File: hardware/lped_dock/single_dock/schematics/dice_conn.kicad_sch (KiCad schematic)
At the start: 3 parts, among them J1 V_{OUT}, J2 CONN, J3 GND

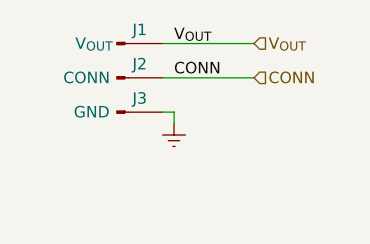
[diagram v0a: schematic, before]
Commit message: feat(hardware): add battery charger and connector to single charger
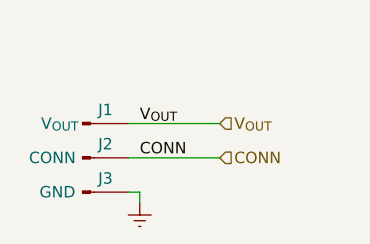
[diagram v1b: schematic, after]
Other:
- moved on the sheet: J1, J2, J3
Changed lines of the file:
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@@
 	(wire
 		(pts
-			(xy 133.35 91.44) (xy 134.62 91.44)
+			(xy 129.54 92.71) (xy 139.7 92.71)
 		)
 		(stroke
@@
 	(wire
 		(pts
-			(xy 143.51 87.63) (xy 133.35 87.63)
+			(xy 139.7 96.52) (xy 129.54 96.52)
 		)
 		(stroke
@@
 	(wire
 		(pts
-			(xy 133.35 83.82) (xy 143.51 83.82)
+			(xy 130.81 100.33) (xy 130.81 101.6)
 		)
 		(stroke
@@
 	(wire
 		(pts
-			(xy 134.62 91.44) (xy 134.62 92.71)
+			(xy 129.54 100.33) (xy 130.81 100.33)
 		)
 		(stroke
@@
 		)
 	)
-	(label "CONN"
-		(at 134.62 87.63 0)
+	(label "V_{OUT}"
+		(at 130.81 92.71 0)
 		(effects
 			(font
@@
 		)
 	)
-	(label "V_{OUT}"
-		(at 134.62 83.82 0)
+	(label "CONN"
+		(at 130.81 96.52 0)
 		(effects
 			(font
@@
 		)
 	)
-	(hierarchical_label "V_{OUT}"
+	(hierarchical_label "CONN"
 		(shape input)
-		(at 143.51 83.82 0)
+		(at 139.7 96.52 0)
 		(effects
 			(font
@@
 		)
 	)
-	(hierarchical_label "CONN"
+	(hierarchical_label "V_{OUT}"
 		(shape input)
-		(at 143.51 87.63 0)
+		(at 139.7 92.71 0)
 		(effects
 			(font
@@
 	(symbol
 		(lib_id "Connector:Conn_01x01_Pin")
-		(at 128.27 87.63 0)
+		(at 124.46 96.52 0)
 		(unit 1)
 		(exclude_from_sim no)
@@
 		(dnp no)
 		(property "Reference" "J2"
-			(at 130.81 86.106 0)
+			(at 127 94.996 0)
 			(effects
 				(font
@@
 		)
 		(property "Value" "CONN"
-			(at 127.508 87.63 0)
+			(at 123.698 96.52 0)
 			(effects
 				(font
@@
 		)
 		(property "Footprint" "Connector_Pin:Pin_D0.9mm_L10.0mm_W2.4mm_FlatFork"
-			(at 128.27 87.63 0)
+			(at 124.46 96.52 0)
 			(effects
 				(font
@@
 		)
 		(property "Datasheet" "~"
-			(at 128.27 87.63 0)
+			(at 124.46 96.52 0)
 			(effects
 				(font
@@
 		)
 		(property "Description" "Generic connector, single row, 01x01, script generated"
-			(at 128.27 87.63 0)
+			(at 124.46 96.52 0)
 			(effects
 				(font
@@
 	(symbol
 		(lib_id "Connector:Conn_01x01_Pin")
-		(at 128.27 83.82 0)
+		(at 124.46 92.71 0)
 		(unit 1)
 		(exclude_from_sim no)
@@
 		(dnp no)
 		(property "Reference" "J1"
-			(at 130.81 82.296 0)
+			(at 127 91.186 0)
 			(effects
 				(font
@@
 		)
 		(property "Value" "V_{OUT}"
-			(at 125.73 83.82 0)
+			(at 121.92 92.71 0)
 			(effects
 				(font
@@
 		)
 		(property "Footprint" "Connector_Pin:Pin_D0.9mm_L10.0mm_W2.4mm_FlatFork"
-			(at 128.27 83.82 0)
+			(at 124.46 92.71 0)
 			(effects
 				(font
@@
 		)
 		(property "Datasheet" "~"
-			(at 128.27 83.82 0)
+			(at 124.46 92.71 0)
 			(effects
 				(font
@@
 		)
 		(property "Description" "Generic connector, single row, 01x01, script generated"
-			(at 128.27 83.82 0)
+			(at 124.46 92.71 0)
 			(effects
 				(font
@@
 	(symbol
 		(lib_id "Connector:Conn_01x01_Pin")
-		(at 128.27 91.44 0)
+		(at 124.46 100.33 0)
 		(unit 1)
 		(exclude_from_sim no)
@@
 		(dnp no)
 		(property "Reference" "J3"
-			(at 130.81 89.916 0)
+			(at 127 98.806 0)
 			(effects
 				(font
@@
 		)
 		(property "Value" "GND"
-			(at 125.476 91.44 0)
+			(at 121.666 100.33 0)
 			(effects
 				(font
@@
 		)
 		(property "Footprint" "Connector_Pin:Pin_D0.9mm_L10.0mm_W2.4mm_FlatFork"
-			(at 128.27 91.44 0)
+			(at 124.46 100.33 0)
 			(effects
 				(font
@@
 		)
 		(property "Datasheet" "~"
-			(at 128.27 91.44 0)
+			(at 124.46 100.33 0)
 			(effects
 				(font
@@
 		)
 		(property "Description" "Generic connector, single row, 01x01, script generated"
-			(at 128.27 91.44 0)
+			(at 124.46 100.33 0)
 			(effects
 				(font
@@
 	(symbol
 		(lib_id "power:Earth")
-		(at 134.62 92.71 0)
+		(at 130.81 101.6 0)
 		(unit 1)
 		(exclude_from_sim no)
@@
 		(fields_autoplaced yes)
 		(property "Reference" "#PWR01"
-			(at 134.62 99.06 0)
+			(at 130.81 107.95 0)
 			(effects
 				(font
@@
 		)
 		(property "Value" "Earth"
-			(at 134.62 97.79 0)
+			(at 130.81 106.68 0)
 			(effects
 				(font
@@
 		)
 		(property "Footprint" ""
-			(at 134.62 92.71 0)
+			(at 130.81 101.6 0)
 			(effects
 				(font
@@
 		)
 		(property "Datasheet" "~"
-			(at 134.62 92.71 0)
+			(at 130.81 101.6 0)
 			(effects
 				(font
@@
 		)
 		(property "Description" "Power symbol creates a global label with name \"Earth\""
-			(at 134.62 92.71 0)
-			(effects
-				(font
+			(at 130.81 101.6 0)
+			(effects
+				(font
